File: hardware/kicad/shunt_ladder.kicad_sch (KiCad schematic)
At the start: 27 parts, among them Q701 IRLML0030, Q702 IRLML0030, Q703 CSD17577Q3A, U701 TC4427EOA, U702 TC4427EOA, U703 MUX509IPWR

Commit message: feat(hardware)!: draw draft A1 of the schematic around a Pico 2
A Raspberry Pi Pico 2 on two 1x20 sockets replaces the ESP32-S3
development board, the programmable logic device and the buffer
between the two boards (D-39 to D-43 of the specification). The former
interface and range logic sheets become two new ones:

- Controller: the Pico 2, the diodes that join its USB supply and the
  5 V rail of the carrier, resistor arrays in the SPI and acquisition
  lines, a reset button and a console header.
- Side Data: two shift registers that take the range, the status
  signals and the eight logic inputs with every sample.

The DUT connects through a 1x4 pin header and a lever terminal block
in parallel, both GND, VIN, VOUT, GND, and the logic port is a 1x10
header with VCC, GND, D7 to D0: the pin order of the PPK2 (D-44). A
solder jumper selects the supply of the DUT side of the level
translator. A transistor at the driver of the ampere switch holds it
open while VIN is above 5.5 V.

Reference designators are numbered as the annotation tool of KiCad
does by default (D-45). The numbering touches every sheet, so these
changes come in one commit. The symbol and the socket footprint of
the ESP32-S3 board leave the project library; the Pico 2 uses the
symbol and the footprint of the KiCad library.

The electrical rules check reports no errors and no warnings. The
parts stay candidates, and no program for the PIO blocks exists yet.

BREAKING CHANGE: the pins of the controller follow the new pin map of
section 5 of the specification.
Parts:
- added R48: 10k, Resistor_SMD:R_0603_1608Metric, symbol Device:R
- renumbered C701 to C46, C702 to C47, C703 to C48, C704 to C49, C706 to C50, C705 to C51, D701 to D7, Q701 to Q6, Q702 to Q7, Q703 to Q8, R712 to R37, R714 to R38, R711 to R39, R713 to R40, R701 to R41, R705 to R42, R702 to R43, R706 to R44, R703 to R45, R707 to R46, R704 to R47, TP701 to TP16, TP702 to TP17, TP703 to TP18, U701 to U15, U702 to U16, U703 to U17
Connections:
- net MUX_EN: no longer names the net of U17.2 (EN)
- net MUX_EN: now also R48.2
- new net +3V3_A: R48.1
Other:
- note added: "Range 0: 1 k (100 uA). Range 1: 33 R (3 mA). Range 2: 1 R (100 mA). Range 3: 0.1 R (1 A). 100 mV full scale each. The shunt of range 0 is always in circuit. No gate-to-source resistors here: they would bypass a shunt. Multiplexer channel 1 = range 0 ... channel 4 = range 3; ranges 2 and 3 use four-terminal parts. Ranges 0 and 1 use the same nets for force and sense: route their sense tracks from 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"
- note removed: "R0 1 k (100 uA), R1 33 R (3 mA), R2 1 R (100 mA), R3 0.1 R (1 A): 100 mV full scale each. R0 is always in circuit. No gate-to-source resistors here: they would bypass a shunt. Multiplexer channel 1 = R0 ... channel 4 = R3; R2 and R3 are four-terminal parts. R0 and R1 use the same nets for force and sense: route their sense tracks from the pads. D701: anti-parallel low-leakage clamp for the first 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"

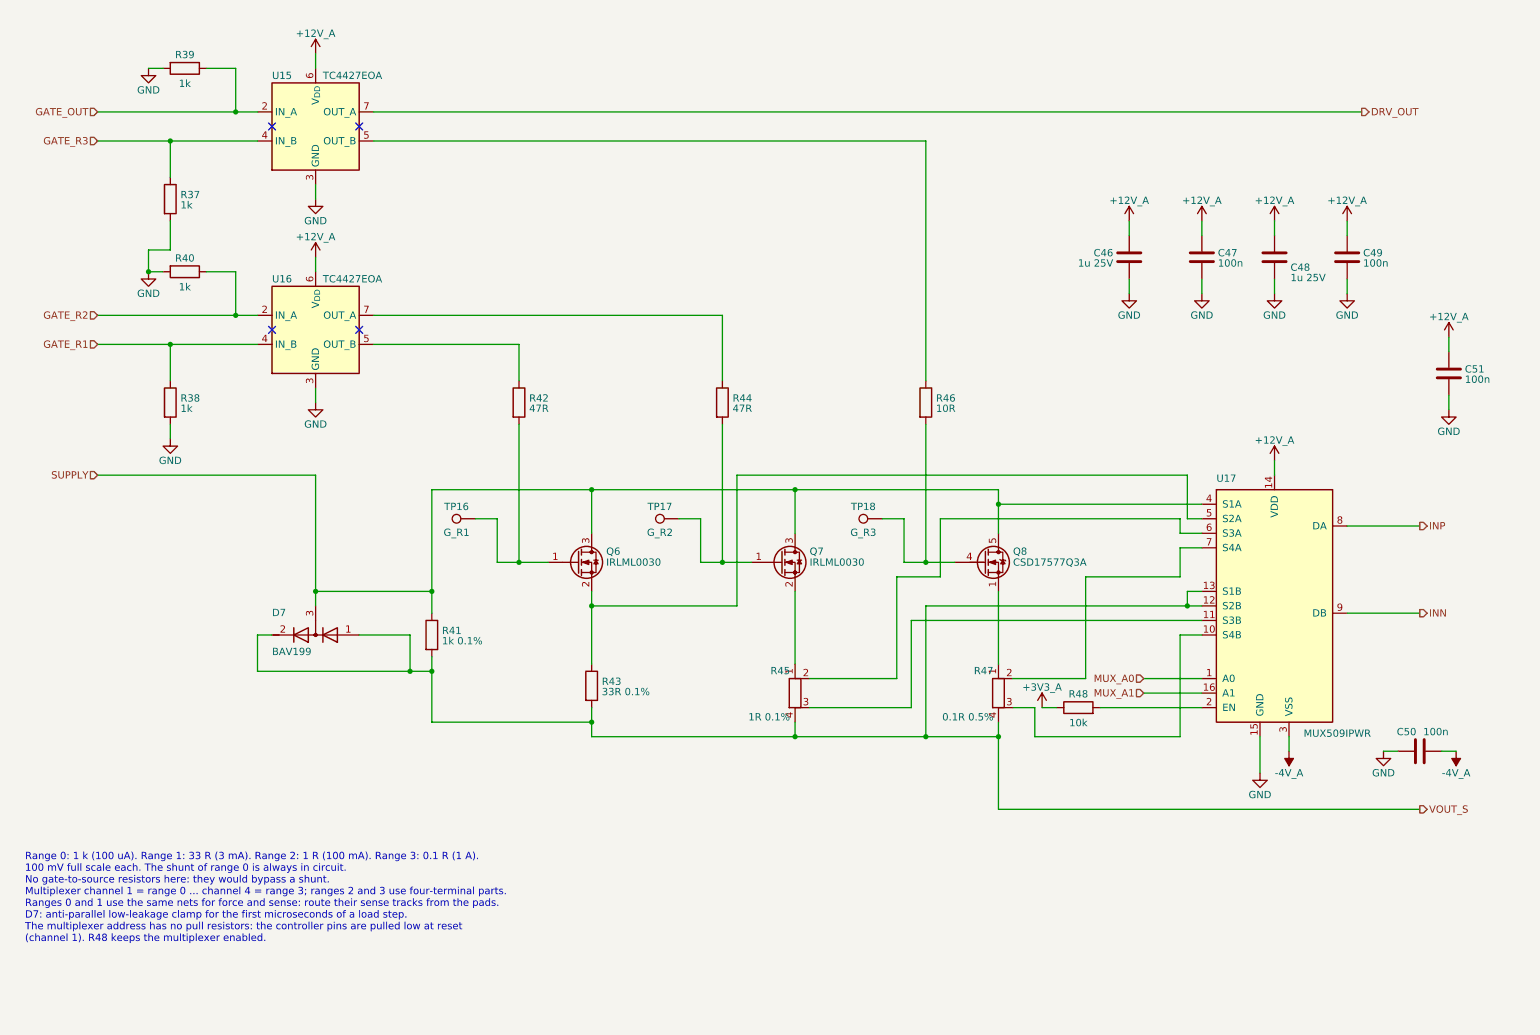
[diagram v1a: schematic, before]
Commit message: feat(hardware): draw draft A2 of the schematic
428 parts on 15 A4 pages, 14 sheets below the root sheet (D-83). Two
sheets are new: Logic Supplies, with the supervisor of the 5 V rail and
the two 3.3 V regulators, and Rail Monitor, with the comparators behind
PWR_GOOD.

The drawings follow the specification of draft A2: a current limiter
on each supply input and a priority multiplexer, a pre-regulator that
tracks the output of the linear regulator, a VIN path that withstands
-20 V to +20 V with its switch open, two diode-connected MOSFETs as
ladder clamp, thin-film and four-terminal shunts, ESD arrays at the CC
pins and at the VCC pin of the logic port. The reference designators
are numbered as KiCad numbers them (D-45), so they are not those of
draft A1.

The project library gains the symbol of the input multiplexer and two
footprints: the lever terminal block with pads of 1.9 mm x 2.3 mm and
the controller module without its antenna keep-out (D-85).

The electrical rules check reports no errors and no warnings. The
parts are candidates, and nothing is built or measured.
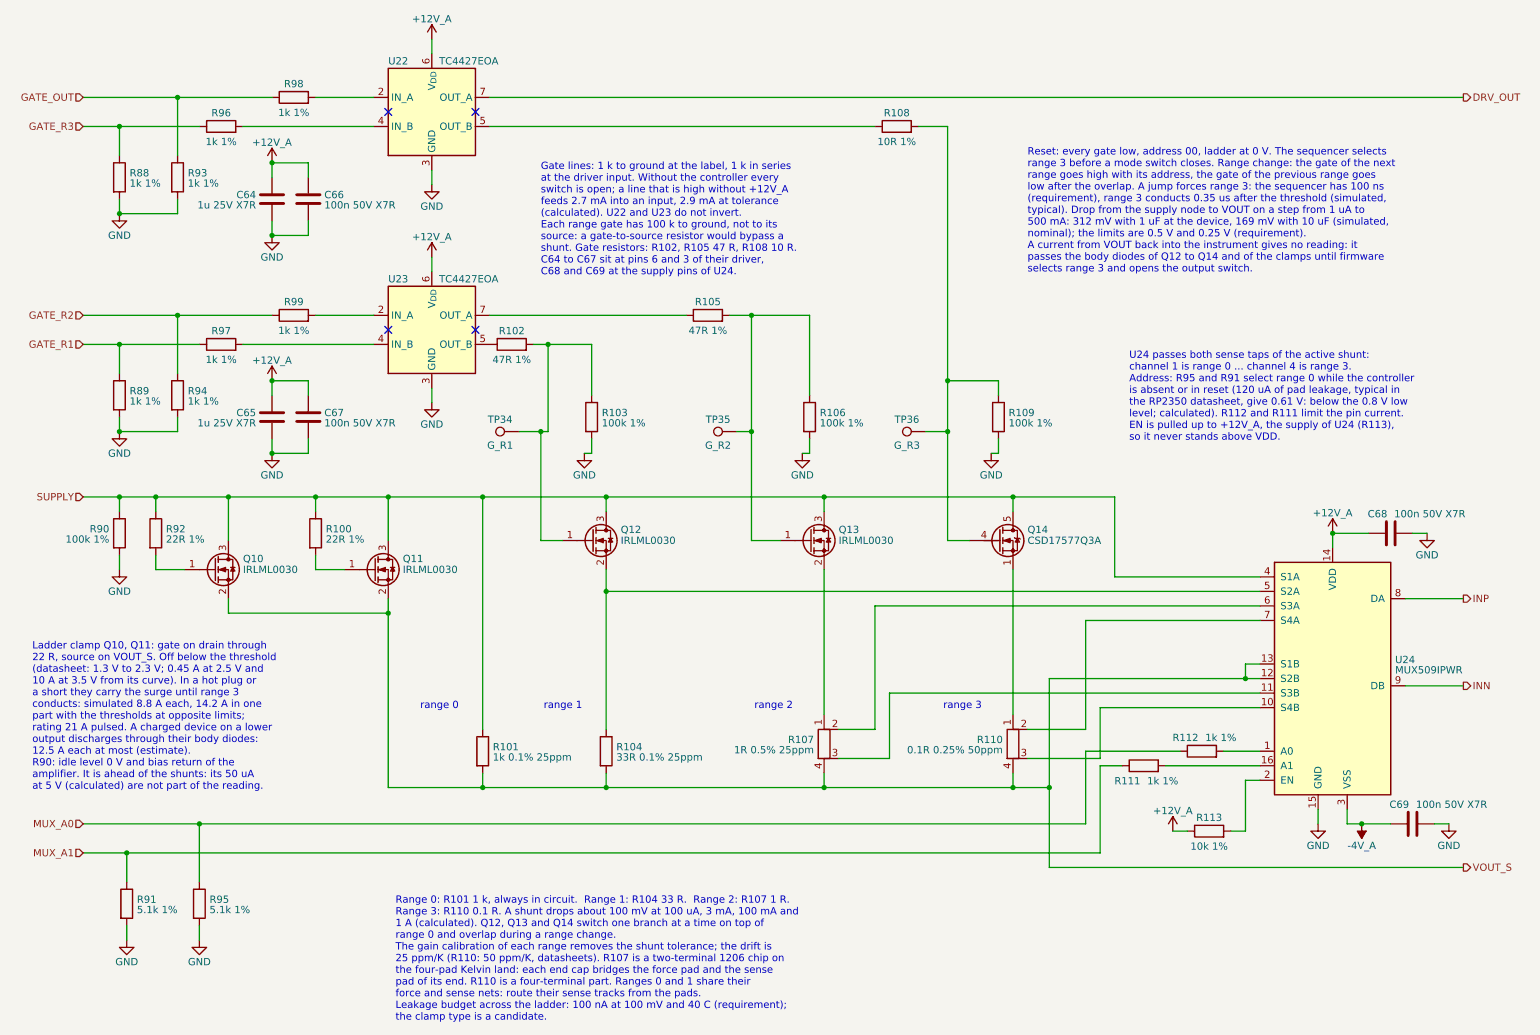
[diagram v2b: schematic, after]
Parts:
- removed D7: BAV199, Package_TO_SOT_SMD:SOT-23, symbol Device:D_Dual_Series_AKC
- added Q10, Q11: IRLML0030, Package_TO_SOT_SMD:SOT-23, symbol Transistor_FET:IRLML0030
- added R100, R92: 22R 1%, Resistor_SMD:R_0603_1608Metric, symbol Device:R
- added R103, R106, R109, R90: 100k 1%, Resistor_SMD:R_0603_1608Metric, symbol Device:R
- added R111, R112, R96, R97, R98, R99: 1k 1%, Resistor_SMD:R_0603_1608Metric, symbol Device:R
- added R91, R95: 5.1k 1%, Resistor_SMD:R_0603_1608Metric, symbol Device:R
- C64: renamed from C46; value 1u 25V -> 1u 25V X7R; MPN (none) -> C0603C105K3RACTU; Manufacturer (none) -> KEMET
- C65: renamed from C48; value 1u 25V -> 1u 25V X7R; MPN (none) -> C0603C105K3RACTU; Manufacturer (none) -> KEMET
- C66: renamed from C47; value 100n -> 100n 50V X7R; MPN (none) -> C0603C104K5RACTU; Manufacturer (none) -> KEMET
- C67: renamed from C49; value 100n -> 100n 50V X7R; MPN (none) -> C0603C104K5RACTU; Manufacturer (none) -> KEMET
- C68: renamed from C51; value 100n -> 100n 50V X7R; MPN (none) -> C0603C104K5RACTU; Manufacturer (none) -> KEMET
- C69: renamed from C50; value 100n -> 100n 50V X7R; MPN (none) -> C0603C104K5RACTU; Manufacturer (none) -> KEMET
- Q12: renamed from Q6; MPN (none) -> IRLML0030TRPBF; Manufacturer (none) -> Infineon
- Q13: renamed from Q7; MPN (none) -> IRLML0030TRPBF; Manufacturer (none) -> Infineon
- Q14: renamed from Q8; MPN (none) -> CSD17577Q3A; Manufacturer (none) -> Texas Instruments
- R101: renamed from R41; value 1k 0.1% -> 1k 0.1% 25ppm; MPN (none) -> TNPW08051K00BEEA; Manufacturer (none) -> Vishay; Note 25 ppm/K -> thin film
- R102: renamed from R42; value 47R -> 47R 1%; MPN (none) -> CRCW060347R0FKEA; Manufacturer (none) -> Vishay
- R104: renamed from R43; value 33R 0.1% -> 33R 0.1% 25ppm; MPN (none) -> CPF0805B33RE1; Manufacturer (none) -> TE Connectivity; Note 25 ppm/K -> thin film, 0.1 W
- R105: renamed from R44; value 47R -> 47R 1%; MPN (none) -> CRCW060347R0FKEA; Manufacturer (none) -> Vishay
- R107: renamed from R45; value 1R 0.1% -> 1R 0.5% 25ppm; MPN (none) -> TNPW12061R00DEEA; Manufacturer (none) -> Vishay; Note four-terminal -> two-terminal 1206 thin-film chip on the Kelvin land; each e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
- R108: renamed from R46; value 10R -> 10R 1%; MPN (none) -> CRCW060310R0FKEA; Manufacturer (none) -> Vishay
- R110: renamed from R47; value 0.1R 0.5% -> 0.1R 0.25% 50ppm; MPN LVK12R100DER -> LVK12R100CER; Manufacturer (none) -> Ohmite; Note (none) -> four-terminal
- R113: renamed from R48; value 10k -> 10k 1%; MPN (none) -> CRCW060310K0FKEA; Manufacturer (none) -> Vishay
- R88: renamed from R37; value 1k -> 1k 1%; MPN (none) -> CRCW06031K00FKEA; Manufacturer (none) -> Vishay
- R89: renamed from R38; value 1k -> 1k 1%; MPN (none) -> CRCW06031K00FKEA; Manufacturer (none) -> Vishay
- R93: renamed from R39; value 1k -> 1k 1%; MPN (none) -> CRCW06031K00FKEA; Manufacturer (none) -> Vishay
- R94: renamed from R40; value 1k -> 1k 1%; MPN (none) -> CRCW06031K00FKEA; Manufacturer (none) -> Vishay
- TP34: renamed from TP16; now left out of the parts list
- TP35: renamed from TP17; now left out of the parts list
- TP36: renamed from TP18; now left out of the parts list
- U22: renamed from U15; MPN (none) -> TC4427EOA713; Manufacturer (none) -> Microchip; Note (none) -> both channels non-inverting
- U23: renamed from U16; MPN (none) -> TC4427EOA713; Manufacturer (none) -> Microchip; Note (none) -> both channels non-inverting
- U24: renamed from U17; MPN (none) -> MUX509IPWR; Manufacturer (none) -> Texas Instruments
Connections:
- net +3V3_A is gone; now on net +12V_A: R113.1
- net GATE_OUT: now also R98.1; no longer U22.2 (IN_A)
- net GATE_R1: now also R97.1; no longer U23.4 (IN_B)
- net GATE_R2: now also R99.1; no longer U23.2 (IN_A)
- net GATE_R3: now also R96.1; no longer U22.4 (IN_B)
- net GND: now also R103.2, R106.2, R109.2, R90.2, R91.2, R95.2
- net MUX_A0: now also R112.1, R95.1; no longer U24.1 (A0)
- net MUX_A1: now also R111.1, R91.1; no longer U24.16 (A1)
- net SUPPLY: now also Q10.3 (D), Q11.3 (D), R100.1, R90.1, R92.1
- net VOUT_S: now also Q10.2 (S), Q11.2 (S)
- net at Q12.1 (G), R102.2, TP34.1: now also R103.1
- net at Q13.1 (G), R105.2, TP35.1: now also R106.1
- net at Q14.4 (G), R108.2, TP36.1: now also R109.1
- new net: Q11.1 (G), R100.2
- new net: Q10.1 (G), R92.2
- new net: R98.2, U22.2 (IN_A)
- new net: R112.2, U24.1 (A0)
- new net: R111.2, U24.16 (A1)
- new net: R97.2, U23.4 (IN_B)
- new net: R96.2, U22.4 (IN_B)
- new net: R99.2, U23.2 (IN_A)
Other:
- note added: "Gate lines: 1 k to ground at the label, 1 k in series at the driver input. Without the controller every switch is open; a line that is high without +12V_A feeds 2.7 mA into an input, 2.9 mA at tolerance (calculated). U22 and U23 do not invert. Each range gate has 100 k to ground, not to its source: a gate-to-source resistor would bypass a shunt. Gate resistors: R102, R105 47 R, R108 10 R. C64 to 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"
- note added: "Ladder clamp Q10, Q11: gate on drain through 22 R, source on VOUT_S. Off below the threshold (datasheet: 1.3 V to 2.3 V; 0.45 A at 2.5 V and 10 A at 3.5 V from its curve). In a hot plug or a short they carry the surge until range 3 conducts: simulated 8.8 A each, 14.2 A in one part with the thresholds at opposite limits; rating 21 A pulsed. A charged device on a lower output discharges through th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"
- note added: "Range 0: R101 1 k, always in circuit. Range 1: R104 33 R. Range 2: R107 1 R. Range 3: R110 0.1 R. A shunt drops about 100 mV at 100 uA, 3 mA, 100 mA and 1 A (calculated). Q12, Q13 and Q14 switch one branch at a time on top of range 0 and overlap during a range change. The gain calibration of each range removes the shunt tolerance; the drift is 25 ppm/K (R110: 50 ppm/K, datasheets). R107 is a two-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"
- note added: "Reset: every gate low, address 00, ladder at 0 V. The sequencer selects range 3 before a mode switch closes. Range change: the gate of the next range goes high with its address, the gate of the previous range goes low after the overlap. A jump forces range 3: the sequencer has 100 ns (requirement), range 3 conducts 0.35 us after the threshold (simulated, typical). Drop from the supply node to VOU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"
- note added: "U24 passes both sense taps of the active shunt: channel 1 is range 0 ... channel 4 is range 3. Address: R95 and R91 select range 0 while the controller is absent or in reset (120 uA of pad leakage, typical in the RP2350 datasheet, give 0.61 V: below the 0.8 V low level; calculated). R112 and R111 limit the pin current. EN is pulled up to +12V_A, the supply of U24 (R113), so it never stands above 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"
- note added: "range 0"
- note added: "range 1"
- note added: "range 2"
- note added: "range 3"
- note removed: "Range 0: 1 k (100 uA). Range 1: 33 R (3 mA). Range 2: 1 R (100 mA). Range 3: 0.1 R (1 A). 100 mV full scale each. The shunt of range 0 is always in circuit. No gate-to-source resistors here: they would bypass a shunt. Multiplexer channel 1 = range 0 ... channel 4 = range 3; ranges 2 and 3 use four-terminal parts. Ranges 0 and 1 use the same nets for force and sense: route their sense tracks from 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"
- moved on the sheet: C64, C65, C66, C67, C68, C69, Q12, Q13, Q14, R101, R102, R104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
